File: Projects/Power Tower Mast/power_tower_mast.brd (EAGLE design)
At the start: 174.1 x 23.1 mm, 54 parts

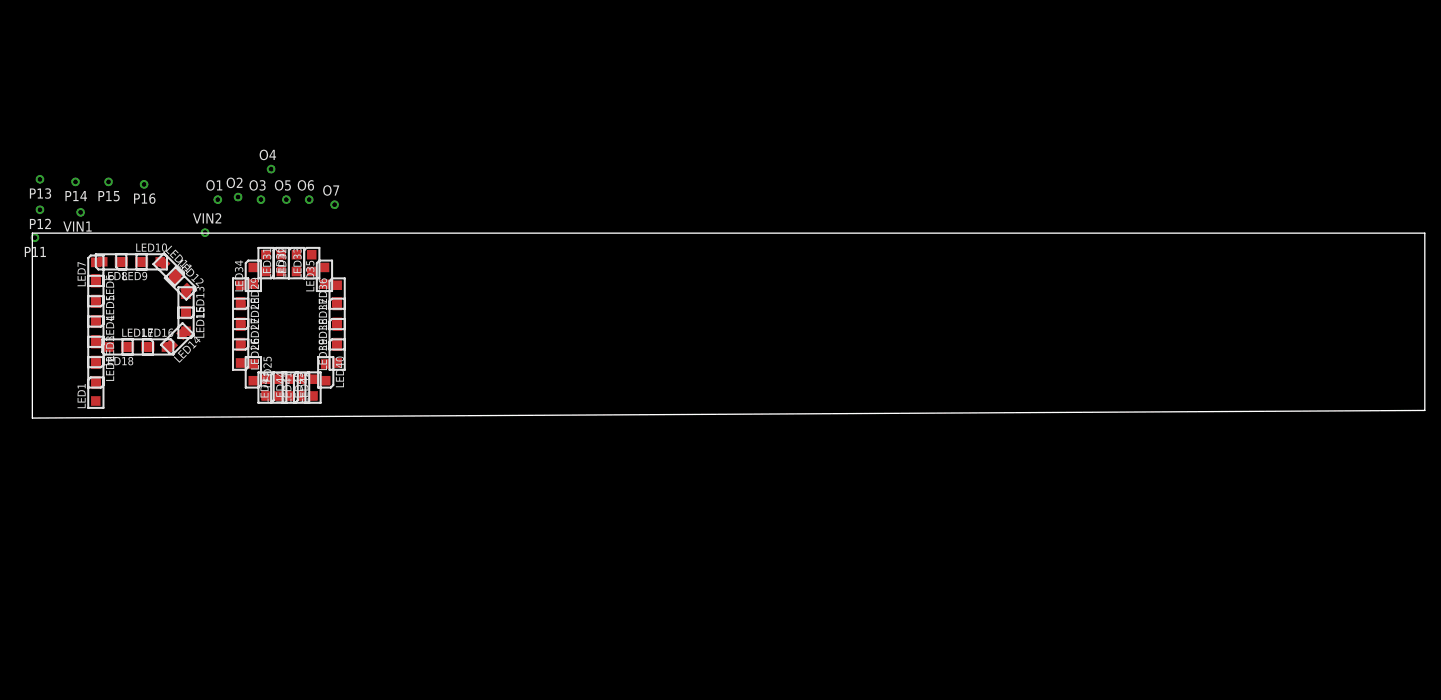
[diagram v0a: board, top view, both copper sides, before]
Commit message: 
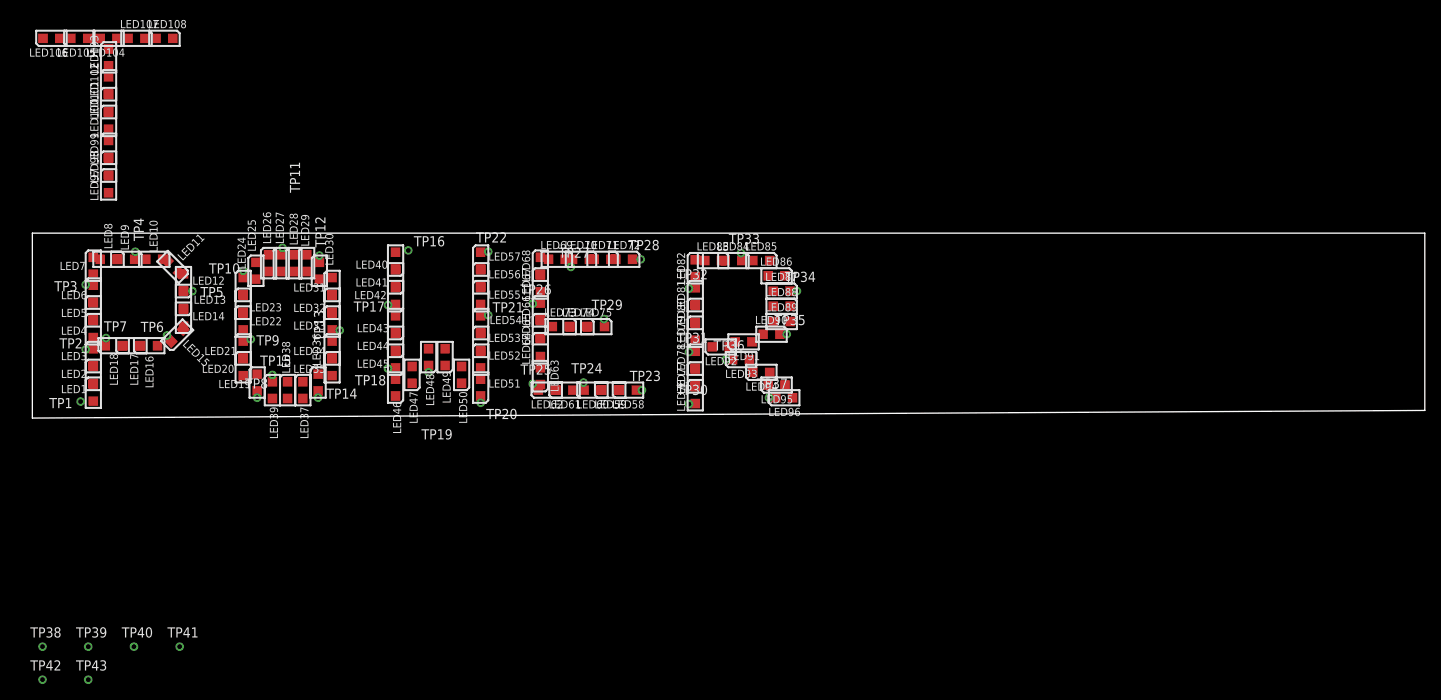
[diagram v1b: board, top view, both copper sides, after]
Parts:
- removed O1, O2, O3, O4, O5, O6, O7, P11, P12, P13, P14, P15, P16, VIN1, VIN2: (no value), CyberRailGuru:P1-20
- added LED100, LED101, LED102, LED103, LED104, LED105, LED106, LED107, LED108, LED19, LED20, LED21, LED22, LED23, LED24, LED46, LED47, LED48, LED49, LED50, LED51, LED52, LED53, LED54, LED55, LED56, LED57, LED58, LED59, LED60, LED61, LED62, LED63, LED64, LED65, LED66, LED67, LED68, LED69, LED70, LED71, LED72, LED73, LED74, LED75, LED76, LED77, LED78, LED79, LED80, LED81, LED82, LED83, LED84, LED85, LED86, LED87, LED88, LED89, LED90, LED91, LED92, LED93, LED94, LED95, LED96, LED97, LED98, LED99: (no value), CyberRailGuru:LED_0805
- added TP1, TP10, TP11, TP12, TP13, TP14, TP15, TP16, TP17, TP18, TP19, TP2, TP20, TP21, TP22, TP23, TP24, TP25, TP26, TP27, TP28, TP29, TP3, TP30, TP31, TP32, TP33, TP34, TP35, TP36, TP37, TP38, TP39, TP4, TP40, TP41, TP42, TP43, TP5, TP6, TP7, TP8, TP9: (no value), CyberRailGuru:P1-20
- moved LED41 18.0 mm to (45.4, 16.5), turned to 180 degrees
- moved LED42 17.4 mm to (45.4, 14.3)
- moved LED44 17.2 mm to (45.4, 8.57)
- moved LED43 16.6 mm to (45.4, 10.8), turned to 180 degrees
- moved LED40 16.5 mm to (45.4, 18.7)
- moved LED34 13.5 mm to (37.5, 7.62)
- moved LED25 12.7 mm to (27.9, 17.5), turned to 0 degrees
- moved LED26 12.0 mm to (29.5, 18.4), turned to 0 degrees
- moved LED35 11.5 mm to (37.5, 5.40)
- moved LED36 11.4 mm to (35.7, 3.49)
- moved LED45 10.9 mm to (45.4, 6.35), turned to 180 degrees
- moved LED37 10.4 mm to (33.8, 2.54)
- moved LED27 10.2 mm to (31.1, 18.4), turned to 0 degrees
- moved LED38 9.33 mm to (31.9, 2.54)
- moved LED39 9.24 mm to (30.0, 2.54)
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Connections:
- removed net VIN: LED12.A, LED15.A, LED18.A, LED3.A, LED6.A, LED9.A, VIN1.TP
- new net N$25: LED41.C, LED42.A
- new net N$26: LED40.C, LED41.A
- new net N$29: LED44.C, LED45.A
- new net N$30: LED43.C, LED44.A
- new net N$31: LED47.C, LED48.A
- new net N$32: LED46.C, LED47.A
- new net N$33: LED50.C, LED51.A
- new net N$34: LED49.C, LED50.A
- new net N$35: LED53.C, LED54.A
- new net N$36: LED52.C, LED53.A
- new net N$37: LED56.C, LED57.A
- new net N$38: LED55.C, LED56.A
- new net N$39: LED59.C, LED60.A
- new net N$40: LED58.C, LED59.A
- new net N$41: LED62.C, LED63.A
- new net N$42: LED61.C, LED62.A
- new net N$43: LED65.C, LED66.A
- new net N$44: LED64.C, LED65.A
- new net N$45: LED68.C, LED69.A
- new net N$46: LED67.C, LED68.A
- new net N$47: LED71.C, LED72.A
- new net N$48: LED70.C, LED71.A
- new net N$49: LED74.C, LED75.A
- new net N$50: LED73.C, LED74.A
- new net N$51: LED77.C, LED78.A
- new net N$52: LED76.C, LED77.A
- new net N$53: LED80.C, LED81.A
- new net N$54: LED79.C, LED80.A
- new net N$55: LED83.C, LED84.A
- new net N$56: LED82.C, LED83.A
- new net N$57: LED86.C, LED87.A
- new net N$58: LED85.C, LED86.A
- new net N$59: LED89.C, LED90.A
- new net N$60: LED88.C, LED89.A
- new net N$61: LED92.C, LED93.A
- new net N$62: LED91.C, LED92.A
- new net N$63: LED95.C, LED96.A
- new net N$64: LED94.C, LED95.A
- new net N$65: LED98.C, LED99.A
- new net N$66: LED97.C, LED98.A
- new net N$67: LED101.C, LED102.A
- new net N$68: LED100.C, LED101.A
- new net N$69: LED104.C, LED105.A
- new net N$70: LED103.C, LED104.A
- new net N$71: LED107.C, LED108.A
- new net N$72: LED106.C, LED107.A
- new net VIN2: LED19.A, LED22.A, LED25.A, LED28.A, LED31.A, LED34.A, LED37.A, TP8.TP
- new net VIN3: LED40.A, LED43.A, LED46.A, LED49.A, LED52.A, LED55.A, TP16.TP
- new net VIN4: LED58.A, LED61.A, LED64.A, LED67.A, LED70.A, LED73.A, TP23.TP
- new net VIN5: LED76.A, LED79.A, LED82.A, LED85.A, LED88.A, LED91.A, LED94.A, TP30.TP
- new net VIN6: LED100.A, LED103.A, LED106.A, LED97.A, TP39.TP
- new net VOUT16: LED48.C, TP19.TP
- new net VOUT17: LED51.C, TP20.TP
- new net VOUT18: LED54.C, TP21.TP
- new net VOUT19: LED57.C, TP22.TP
- new net VOUT20: LED60.C, TP24.TP
- new net VOUT21: LED63.C, TP25.TP
- new net VOUT22: LED66.C, TP26.TP
- new net VOUT23: LED69.C, TP27.TP
- new net VOUT24: LED72.C, TP28.TP
- new net VOUT25: LED75.C, TP29.TP
- new net VOUT26: LED78.C, TP31.TP
- new net VOUT27: LED81.C, TP32.TP
- new net VOUT28: LED84.C, TP33.TP
- new net VOUT29: LED87.C, TP34.TP
- new net VOUT30: LED90.C, TP35.TP
- new net VOUT31: LED93.C, TP36.TP
- new net VOUT32: LED96.C, TP37.TP
- new net VOUT33: LED99.C, TP40.TP
- new net VOUT34: LED102.C, TP41.TP
- new net VOUT35: LED105.C, TP42.TP
- new net VOUT36: LED108.C, TP43.TP
- new net VOUT7: LED21.C, TP9.TP
- new net VOUT8: LED24.C, TP10.TP
- net N$1: now also LED3.A; no longer LED1.A
- net N$10: now also LED7.C; no longer LED9.C
- net N$11: now also LED26.C, LED27.A; no longer LED31.A, LED32.C
- net N$12: now also LED25.C, LED26.A; no longer LED32.A, LED33.C
- net N$13: now also LED12.A; no longer LED10.A
- net N$14: now also LED10.C; no longer LED12.C
- net N$15: now also LED29.C, LED30.A; no longer LED34.A, LED35.C
- net N$16: now also LED28.C, LED29.A; no longer LED35.A, LED36.C
- net N$17: now also LED15.A; no longer LED13.A
- net N$18: now also LED13.C; no longer LED15.C
- net N$19: now also LED32.C, LED33.A; no longer LED37.A, LED38.C
- net N$2: now also LED1.C; no longer LED3.C
- net N$20: now also LED31.C, LED32.A; no longer LED38.A, LED39.C
- net N$21: now also LED18.A; no longer LED16.A
- net N$22: now also LED16.C; no longer LED18.C
- net N$23: now also LED35.C, LED36.A; no longer LED40.A, LED41.C
- net N$24: now also LED34.C, LED35.A; no longer LED41.A, LED42.C
- net N$27: now also LED38.C, LED39.A; no longer LED43.A, LED44.C
- net N$28: now also LED37.C, LED38.A; no longer LED44.A, LED45.C
- net N$3: now also LED20.C, LED21.A; no longer LED25.A, LED26.C
- net N$4: now also LED19.C, LED20.A; no longer LED26.A, LED27.C
- net N$5: now also LED6.A; no longer LED4.A
- net N$6: now also LED4.C; no longer LED6.C
- net N$7: now also LED23.C, LED24.A; no longer LED28.A, LED29.C
- net N$8: now also LED22.C, LED23.A; no longer LED29.A, LED30.C
- net N$9: now also LED9.A; no longer LED7.A
- net VIN1: now also LED1.A, LED10.A, LED13.A, LED16.A, LED4.A, LED7.A, TP1.TP; no longer LED27.A, LED30.A, LED33.A, LED36.A, LED39.A, LED42.A, LED45.A, VIN2.TP
- net VOUT1: now also LED3.C, TP2.TP; no longer LED1.C, P11.TP
- net VOUT10: now also LED30.C, TP12.TP; no longer LED28.C, O2.TP
- net VOUT11: now also LED33.C, TP13.TP; no longer LED31.C, O3.TP
- net VOUT12: now also LED36.C, TP14.TP; no longer LED34.C, O4.TP
- net VOUT13: now also LED39.C, TP15.TP; no longer LED37.C, O5.TP
- net VOUT14: now also LED42.C, TP17.TP; no longer LED40.C, O6.TP
- net VOUT15: now also LED45.C, TP18.TP; no longer LED43.C, O7.TP
- net VOUT2: now also LED6.C, TP3.TP; no longer LED4.C, P12.TP
- net VOUT3: now also LED9.C, TP4.TP; no longer LED7.C, P13.TP
- net VOUT4: now also LED12.C, TP5.TP; no longer LED10.C, P14.TP
- net VOUT5: now also LED15.C, TP6.TP; no longer LED13.C, P15.TP
- net VOUT6: now also LED18.C, TP7.TP; no longer LED16.C, P16.TP
- net VOUT9: now also LED27.C, TP11.TP; no longer LED25.C, O1.TP
